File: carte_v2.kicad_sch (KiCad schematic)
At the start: 25 parts, among them J1 Conn_01x03_Socket, J2 Conn_01x04_Socket, J3 Conn_01x03_Socket, J4 Conn_01x03_Socket, J5 Conn_01x04_Socket, J6 Conn_01x03_Socket, J7 Conn_02x20_Odd_Even, J8 Conn_01x04_Socket, J9 Conn_01x04_Socket, SW1 SW_Push_Dual, SW2 SW_Push_Dual, SW3 SW_Push_Dual, U1 Arduino_Nano

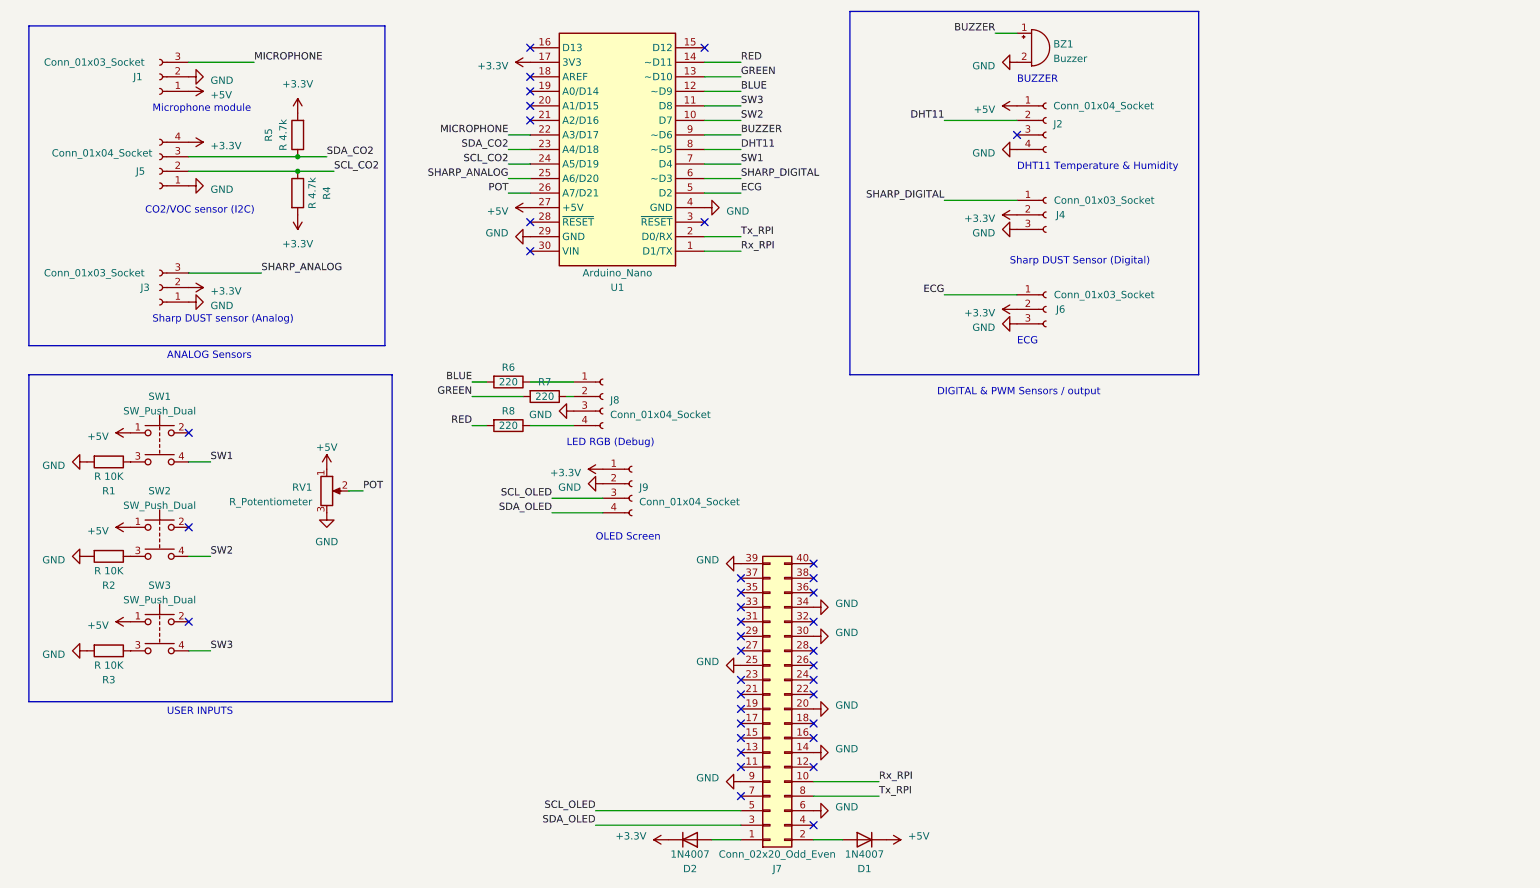
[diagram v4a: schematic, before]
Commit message: almost finished routing (missing buttons)
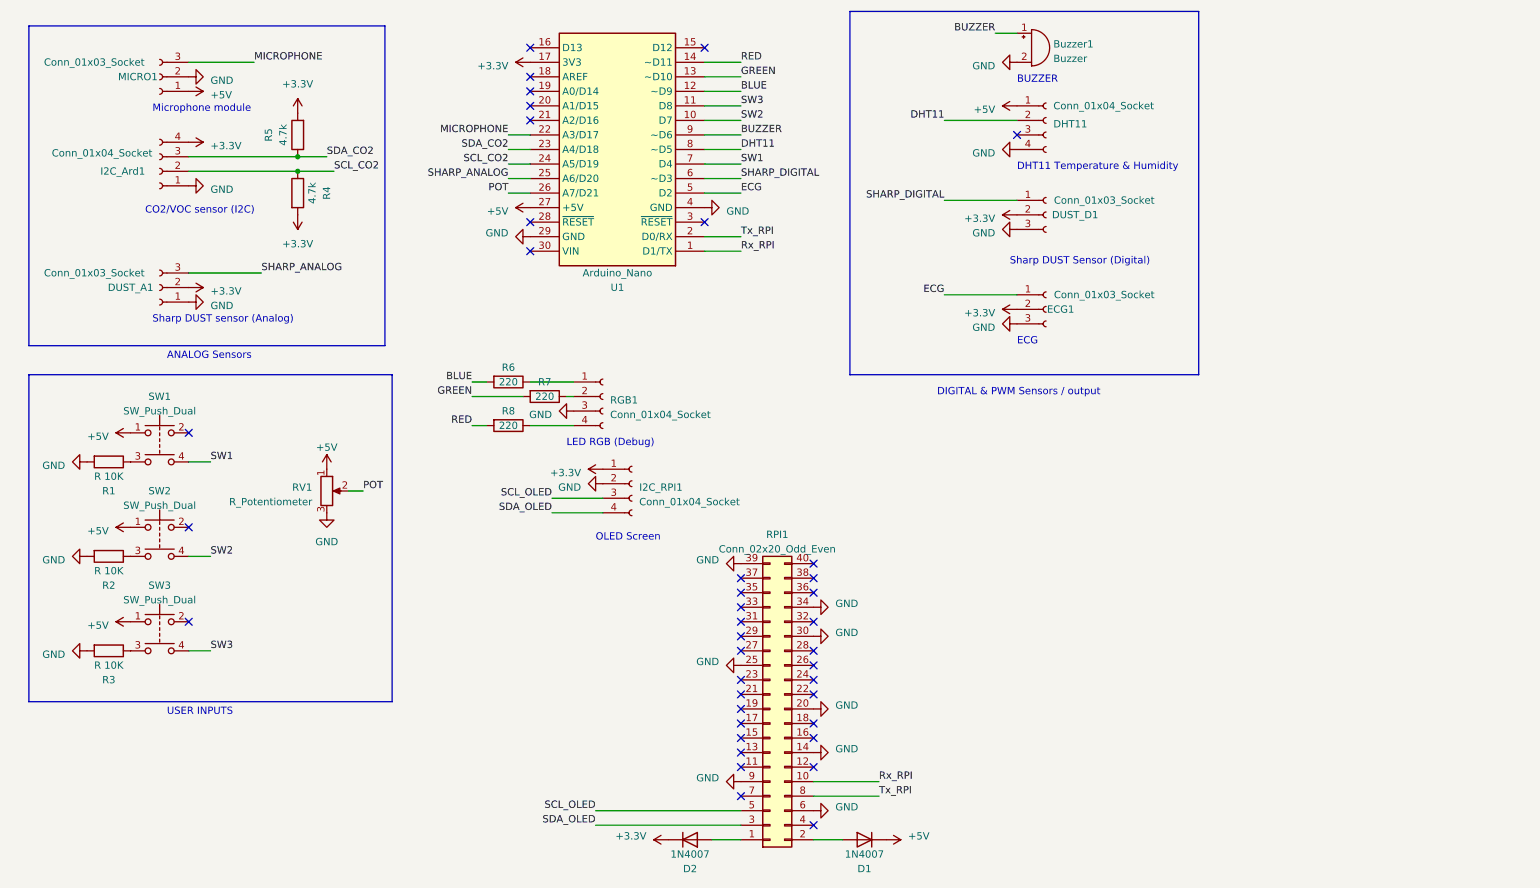
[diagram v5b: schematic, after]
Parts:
- R4, R5: value R 4.7k -> 4.7k
- renumbered BZ1 to Buzzer1, J2 to DHT11, J3 to DUST_A1, J4 to DUST_D1, J6 to ECG1, J5 to I2C_Ard1, J9 to I2C_RPI1, J1 to MICRO1, J8 to RGB1, J7 to RPI1
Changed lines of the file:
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@@
   (symbol (lib_id "Connector:Conn_01x03_Socket") (at 38.1 25.4 180) (unit 1)
     (in_bom yes) (on_board yes) (dnp no)
-    (property "Reference" "J1" (at 34.29 25.4 0)
+    (property "Reference" "MICRO1" (at 34.29 25.4 0)
       (effects (font (size 1.27 1.27)))
     )
@@
       (project "carte_v2"
         (path "/05d1f801-cf8d-4e41-b501-4418fad4fef4"
-          (reference "J1") (unit 1)
+          (reference "MICRO1") (unit 1)
         )
       )
@@
   (symbol (lib_id "Connector:Conn_01x03_Socket") (at 193.04 66.04 0) (unit 1)
     (in_bom yes) (on_board yes) (dnp no)
-    (property "Reference" "J6" (at 195.58 66.04 0)
+    (property "Reference" "ECG1" (at 195.58 66.04 0)
       (effects (font (size 1.27 1.27)))
     )
@@
       (project "carte_v2"
         (path "/05d1f801-cf8d-4e41-b501-4418fad4fef4"
-          (reference "J6") (unit 1)
+          (reference "ECG1") (unit 1)
         )
       )
@@
       (effects (font (size 1.27 1.27)))
     )
-    (property "Value" "R 4.7k " (at 64.77 45.72 90)
+    (property "Value" "4.7k " (at 64.77 45.72 90)
       (effects (font (size 1.27 1.27)))
     )
@@
   (symbol (lib_id "Connector:Conn_01x04_Socket") (at 120.65 96.52 0) (unit 1)
     (in_bom yes) (on_board yes) (dnp no) (fields_autoplaced)
-    (property "Reference" "J9" (at 121.92 97.155 0)
+    (property "Reference" "I2C_RPI1" (at 121.92 97.155 0)
       (effects (font (size 1.27 1.27)) (justify left))
     )
@@
       (project "carte_v2"
         (path "/05d1f801-cf8d-4e41-b501-4418fad4fef4"
-          (reference "J9") (unit 1)
+          (reference "I2C_RPI1") (unit 1)
         )
       )
@@
       (effects (font (size 1.27 1.27)))
     )
-    (property "Value" "R 4.7k " (at 59.69 35.56 90)
+    (property "Value" "4.7k " (at 59.69 35.56 90)
       (effects (font (size 1.27 1.27)))
     )
@@
   (symbol (lib_id "Connector:Conn_01x04_Socket") (at 193.04 33.02 0) (unit 1)
     (in_bom yes) (on_board yes) (dnp no)
-    (property "Reference" "J2" (at 194.31 33.655 0)
+    (property "Reference" "DHT11" (at 194.31 33.655 0)
       (effects (font (size 1.27 1.27)) (justify left))
     )
@@
       (project "carte_v2"
         (path "/05d1f801-cf8d-4e41-b501-4418fad4fef4"
-          (reference "J2") (unit 1)
+          (reference "DHT11") (unit 1)
         )
       )
@@
   (symbol (lib_id "Device:Buzzer") (at 190.5 20.32 0) (unit 1)
     (in_bom yes) (on_board yes) (dnp no) (fields_autoplaced)
-    (property "Reference" "BZ1" (at 194.31 19.685 0)
+    (property "Reference" "Buzzer1" (at 194.31 19.685 0)
       (effects (font (size 1.27 1.27)) (justify left))
     )
@@
       (project "carte_v2"
         (path "/05d1f801-cf8d-4e41-b501-4418fad4fef4"
-          (reference "BZ1") (unit 1)
+          (reference "Buzzer1") (unit 1)
         )
       )
@@
   (symbol (lib_id "Connector:Conn_01x04_Socket") (at 115.57 81.28 0) (unit 1)
     (in_bom yes) (on_board yes) (dnp no) (fields_autoplaced)
-    (property "Reference" "J8" (at 116.84 81.915 0)
+    (property "Reference" "RGB1" (at 116.84 81.915 0)
       (effects (font (size 1.27 1.27)) (justify left))
     )
@@
       (project "carte_v2"
         (path "/05d1f801-cf8d-4e41-b501-4418fad4fef4"
-          (reference "J8") (unit 1)
+          (reference "RGB1") (unit 1)
         )
       )
@@
   (symbol (lib_id "Connector:Conn_01x03_Socket") (at 38.1 62.23 180) (unit 1)
     (in_bom yes) (on_board yes) (dnp no)
-    (property "Reference" "J3" (at 35.56 62.23 0)
+    (property "Reference" "DUST_A1" (at 33.02 62.23 0)
       (effects (font (size 1.27 1.27)))
     )
@@
       (project "carte_v2"
         (path "/05d1f801-cf8d-4e41-b501-4418fad4fef4"
-          (reference "J3") (unit 1)
+          (reference "DUST_A1") (unit 1)
         )
       )
@@
   (symbol (lib_id "Connector_Generic:Conn_02x20_Odd_Even") (at 144.78 135.89 0) (mirror x) (unit 1)
     (in_bom yes) (on_board yes) (dnp no) (fields_autoplaced)
-    (property "Reference" "J7" (at 146.05 163.83 0)
-      (effects (font (size 1.27 1.27)))
-    )
-    (property "Value" "Conn_02x20_Odd_Even" (at 146.05 161.29 0)
+    (property "Reference" "RPI1" (at 146.05 105.41 0)
+      (effects (font (size 1.27 1.27)))
+    )
+    (property "Value" "Conn_02x20_Odd_Even" (at 146.05 107.95 0)
       (effects (font (size 1.27 1.27)))
     )
@@
       (project "carte_v2"
         (path "/05d1f801-cf8d-4e41-b501-4418fad4fef4"
-          (reference "J7") (unit 1)
+          (reference "RPI1") (unit 1)
         )
       )
@@
   (symbol (lib_id "Connector:Conn_01x03_Socket") (at 193.04 49.53 0) (unit 1)
     (in_bom yes) (on_board yes) (dnp no)
-    (property "Reference" "J4" (at 195.58 49.53 0)
+    (property "Reference" "DUST_D1" (at 198.12 49.53 0)
       (effects (font (size 1.27 1.27)))
     )
@@
       (project "carte_v2"
         (path "/05d1f801-cf8d-4e41-b501-4418fad4fef4"
-          (reference "J4") (unit 1)
+          (reference "DUST_D1") (unit 1)
         )
       )
@@
   (symbol (lib_id "Connector:Conn_01x04_Socket") (at 38.1 41.91 180) (unit 1)
     (in_bom yes) (on_board yes) (dnp no)
-    (property "Reference" "J5" (at 35.56 41.91 0)
+    (property "Reference" "I2C_Ard1" (at 35.56 41.91 0)
       (effects (font (size 1.27 1.27)) (justify left))
     )
@@
       (project "carte_v2"
         (path "/05d1f801-cf8d-4e41-b501-4418fad4fef4"
-          (reference "J5") (unit 1)
-        )
-      )
+          (reference "I2C_Ard1") (unit 1)
+        )
+      )

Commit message: routing finished, need to resolve error
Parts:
- SW1, SW2, SW3: footprint Button_Switch_THT:SW_PUSH_6mm_H5mm -> Button_Switch_THT:SW_PUSH_6mm_H5mm_PATCHED
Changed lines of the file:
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@@
       (effects (font (size 1.27 1.27)))
     )
-    (property "Footprint" "Button_Switch_THT:SW_PUSH_6mm_H5mm" (at 38.1 99.06 0)
+    (property "Footprint" "Button_Switch_THT:SW_PUSH_6mm_H5mm_PATCHED" (at 38.1 99.06 0)
       (effects (font (size 1.27 1.27)) hide)
     )
@@
       (effects (font (size 1.27 1.27)))
     )
-    (property "Footprint" "Button_Switch_THT:SW_PUSH_6mm_H5mm" (at 38.1 82.55 0)
+    (property "Footprint" "Button_Switch_THT:SW_PUSH_6mm_H5mm_PATCHED" (at 38.1 82.55 0)
       (effects (font (size 1.27 1.27)) hide)
     )
@@
       (effects (font (size 1.27 1.27)))
     )
-    (property "Footprint" "Button_Switch_THT:SW_PUSH_6mm_H5mm" (at 38.1 115.57 0)
-      (effects (font (size 1.27 1.27)) hide)
-    )
+    (property "Footprint" "Button_Switch_THT:SW_PUSH_6mm_H5mm_PATCHED" (at 38.1 115.57 0)
+      (effects (font (size 1.27 1.27)) hide)
+    )

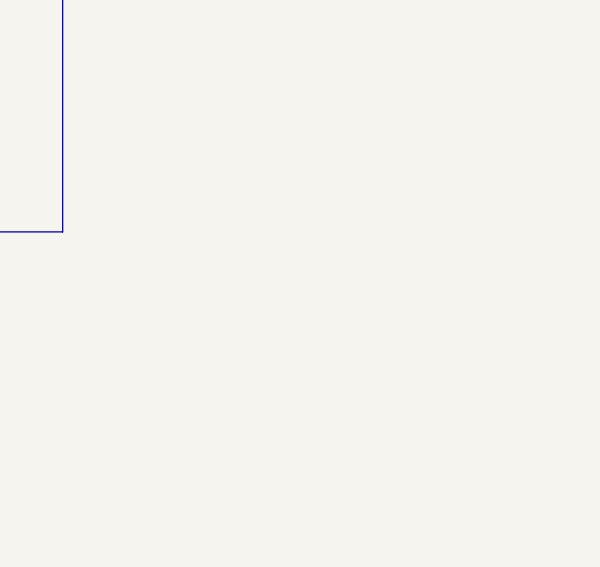
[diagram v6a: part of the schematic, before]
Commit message: added mouting hole + routing over with no error
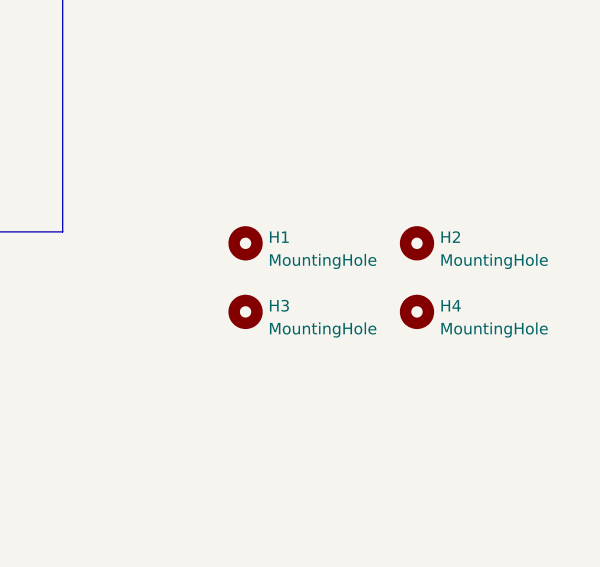
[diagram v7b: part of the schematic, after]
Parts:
- added H1, H2, H3, H4: MountingHole, MountingHole:MountingHole_3mm, symbol Mechanical:MountingHole
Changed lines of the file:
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@@
+    )
+  )
+  (symbol (lib_id "Mechanical:MountingHole") (at 259.08 86.36 0) (unit 1)
+    (in_bom yes) (on_board yes) (dnp no) (fields_autoplaced)
+    (property "Reference" "H4" (at 261.62 85.725 0)
+      (effects (font (size 1.27 1.27)) (justify left))
+    )
+    (property "Value" "MountingHole" (at 261.62 88.265 0)
+      (effects (font (size 1.27 1.27)) (justify left))
+    )
+    (property "Footprint" "MountingHole:MountingHole_3mm" (at 259.08 86.36 0)
+      (effects (font (size 1.27 1.27)) hide)
+    )
+    (property "Datasheet" "~" (at 259.08 86.36 0)
+      (effects (font (size 1.27 1.27)) hide)
+    )
+    (instances
+      (project "carte_v2"
+        (path "/05d1f801-cf8d-4e41-b501-4418fad4fef4"
+          (reference "H4") (unit 1)
+        )
+      )
     )
   )
@@
     )
   )
+  (symbol (lib_id "Mechanical:MountingHole") (at 259.08 78.74 0) (unit 1)
+    (in_bom yes) (on_board yes) (dnp no) (fields_autoplaced)
+    (property "Reference" "H2" (at 261.62 78.105 0)
+      (effects (font (size 1.27 1.27)) (justify left))
+    )
+    (property "Value" "MountingHole" (at 261.62 80.645 0)
+      (effects (font (size 1.27 1.27)) (justify left))
+    )
+    (property "Footprint" "MountingHole:MountingHole_3mm" (at 259.08 78.74 0)
+      (effects (font (size 1.27 1.27)) hide)
+    )
+    (property "Datasheet" "~" (at 259.08 78.74 0)
+      (effects (font (size 1.27 1.27)) hide)
+    )
+    (instances
+      (project "carte_v2"
+        (path "/05d1f801-cf8d-4e41-b501-4418fad4fef4"
+          (reference "H2") (unit 1)
+        )
+      )
+    )
+  )
   (symbol (lib_id "Device:R") (at 29.21 125.73 270) (unit 1)
     (in_bom yes) (on_board yes) (dnp no)
@@
         (path "/05d1f801-cf8d-4e41-b501-4418fad4fef4"
           (reference "#PWR06") (unit 1)
+        )
+      )
+    )
+  )
+  (symbol (lib_id "Mechanical:MountingHole") (at 240.03 78.74 0) (unit 1)
+    (in_bom yes) (on_board yes) (dnp no) (fields_autoplaced)
+    (property "Reference" "H1" (at 242.57 78.105 0)
+      (effects (font (size 1.27 1.27)) (justify left))
+    )
+    (property "Value" "MountingHole" (at 242.57 80.645 0)
+      (effects (font (size 1.27 1.27)) (justify left))
+    )
+    (property "Footprint" "MountingHole:MountingHole_3mm" (at 240.03 78.74 0)
+      (effects (font (size 1.27 1.27)) hide)
+    )
+    (property "Datasheet" "~" (at 240.03 78.74 0)
+      (effects (font (size 1.27 1.27)) hide)
+    )
+    (instances
+      (project "carte_v2"
+        (path "/05d1f801-cf8d-4e41-b501-4418fad4fef4"
+          (reference "H1") (unit 1)
         )
       )
@@
         )
       )
+    )
+  )
+  (symbol (lib_id "Mechanical:MountingHole") (at 240.03 86.36 0) (unit 1)
+    (in_bom yes) (on_board yes) (dnp no) (fields_autoplaced)
+    (property "Reference" "H3" (at 242.57 85.725 0)
+      (effects (font (size 1.27 1.27)) (justify left))
+    )
+    (property "Value" "MountingHole" (at 242.57 88.265 0)
+      (effects (font (size 1.27 1.27)) (justify left))
+    )
+    (property "Footprint" "MountingHole:MountingHole_3mm" (at 240.03 86.36 0)
+      (effects (font (size 1.27 1.27)) hide)
+    )
+    (property "Datasheet" "~" (at 240.03 86.36 0)
+      (effects (font (size 1.27 1.27)) hide)
+    )
+    (instances
+      (project "carte_v2"
+        (path "/05d1f801-cf8d-4e41-b501-4418fad4fef4"
+          (reference "H3") (unit 1)
+        )
+      )

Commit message: remake rpi footprint
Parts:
- RPI1: footprint Connector_PinHeader_2.00mm:PinHeader_2x20_P2.00mm_Vertical -> Connector_PinHeader_2.54mm:PinHeader_2x20_P2.54mm_Vertical
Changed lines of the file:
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@@
       (effects (font (size 1.27 1.27)))
     )
-    (property "Footprint" "Connector_PinHeader_2.00mm:PinHeader_2x20_P2.00mm_Vertical" (at 144.78 135.89 0)
+    (property "Footprint" "Connector_PinHeader_2.54mm:PinHeader_2x20_P2.54mm_Vertical" (at 144.78 135.89 0)
       (effects (font (size 1.27 1.27)) hide)
     )
